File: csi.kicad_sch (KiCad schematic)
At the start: 38 parts, among them J6 WE_68715014522, J7 WE_68715014022, T8 BSS138APW, U4 PCA9547BS,118

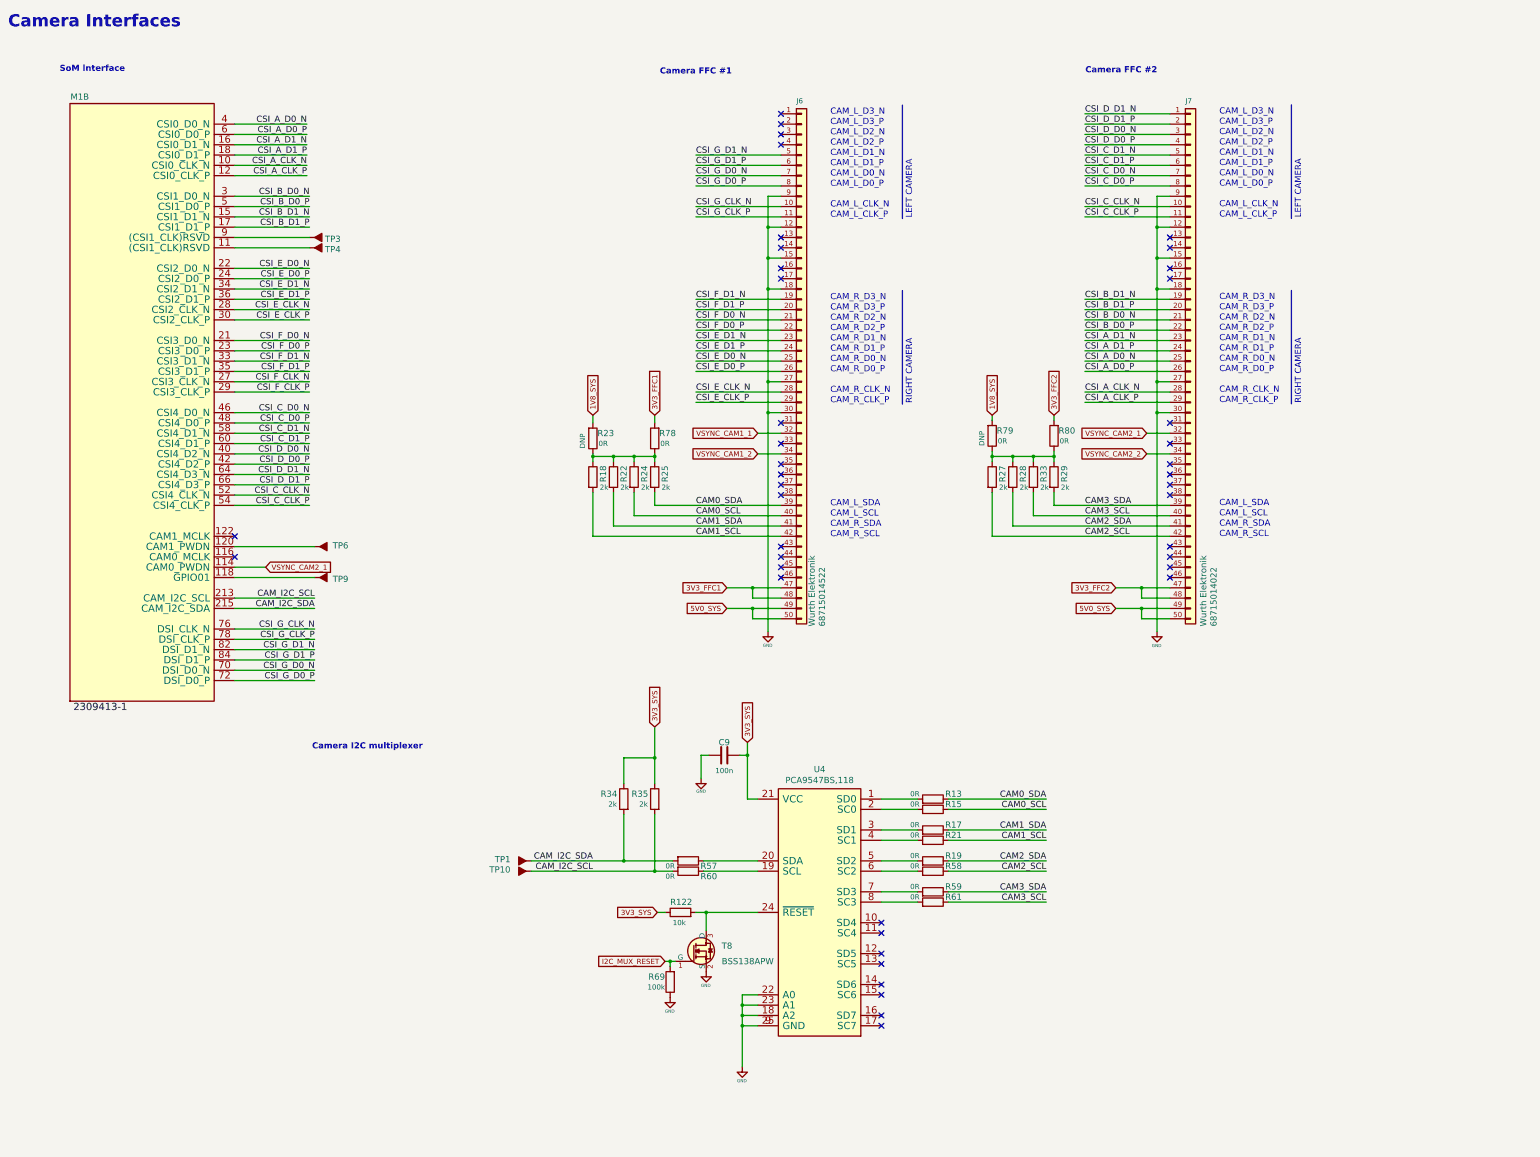
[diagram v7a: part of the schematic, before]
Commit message: Standardize components
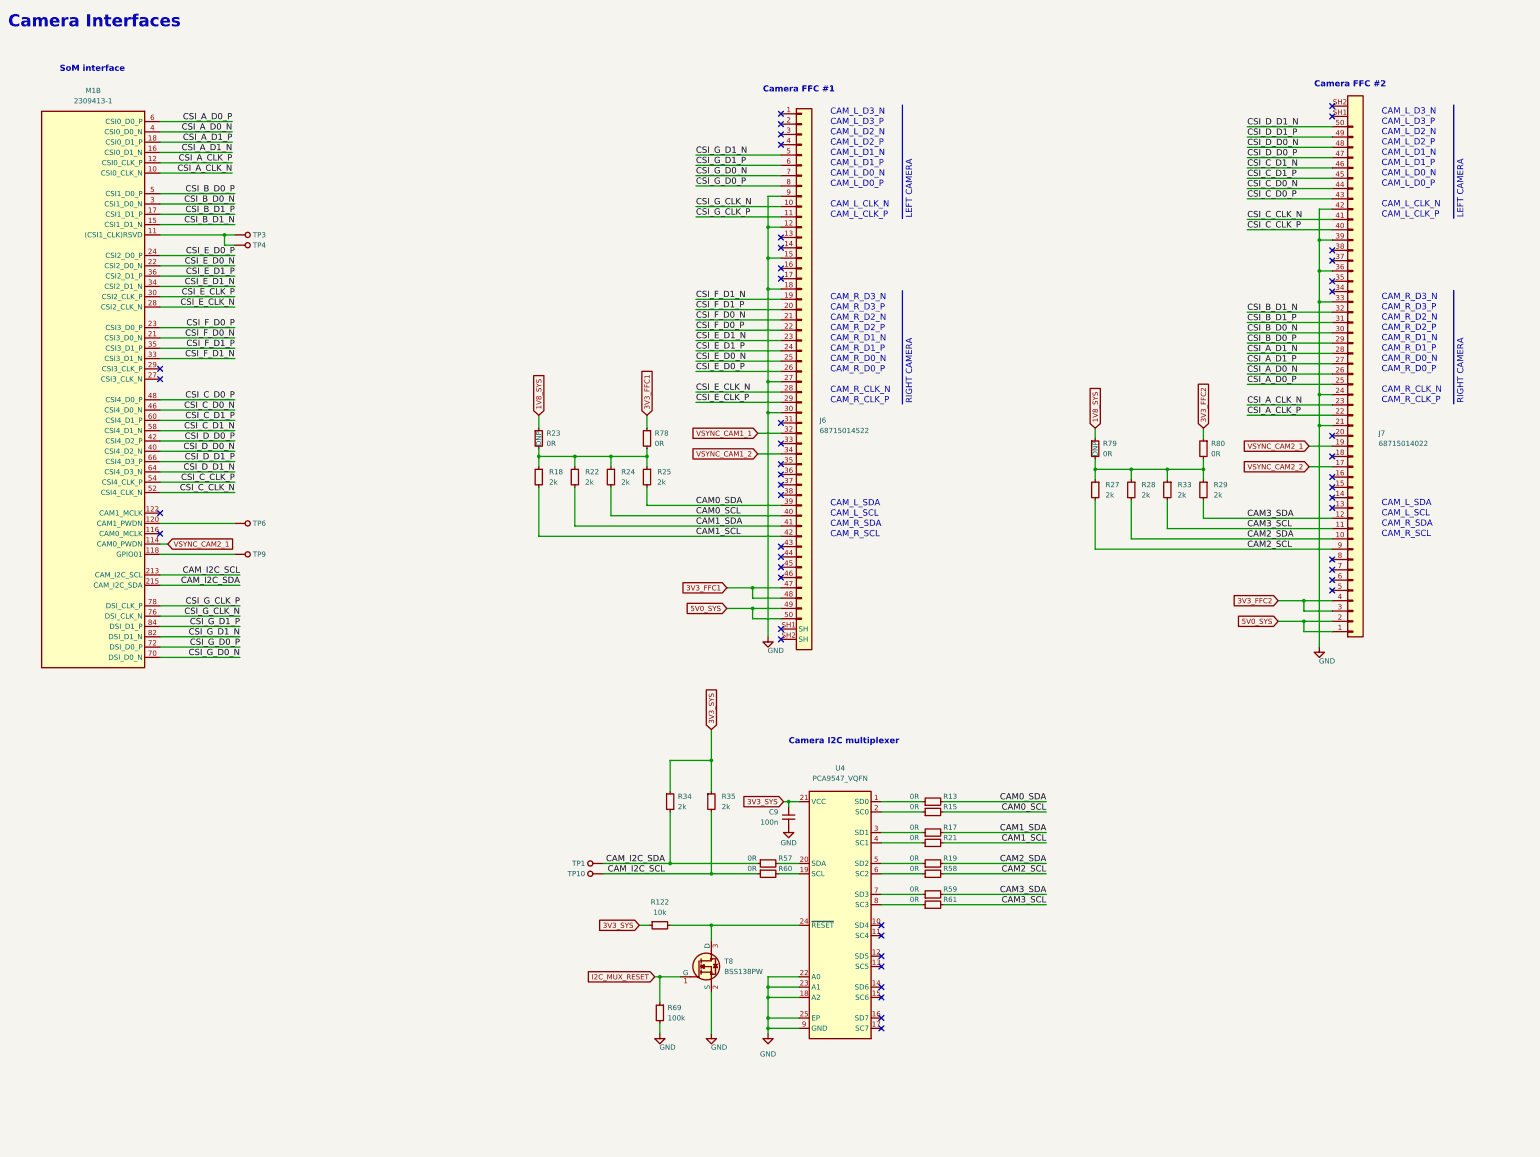
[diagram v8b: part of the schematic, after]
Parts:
- removed J6: WE_68715014522, jetson-nano-baseboard-footprints:WE_68715014522_ONE-SIDE, symbol jetson-nano-baseboard:WE_68715014522
- removed J7: WE_68715014022, jetson-nano-baseboard-footprints:WE_68715014022, symbol jetson-nano-baseboard:WE_68715014022
- removed U4: PCA9547BS,118, jetson-nano-baseboard-footprints:HVQFN24, symbol jetson-nano-baseboard:PCA9547BS,118
- added J6: Conn_FFC_WE_68715014522_ONE-SIDE, antmicro-footprints:Conn_FFC_WE_68715014x22, symbol antmicroFCCConnectors:Conn_FFC_WE_68715014522_ONE-SIDE
- added J7: Conn_FFC_WE_68715014022_ONE-SIDE, antmicro-footprints:Conn_FFC_WE_68715014x22, symbol antmicroFCCConnectors:Conn_FFC_WE_68715014022_ONE-SIDE
- added U4: PCA9547_VQFN, antmicro-footprints:VQFN-24-1EP_3.8x3.8x1.0mm_P0.5mm, symbol antmicroLogicSignalSwitchesMultiplexersDecoders:PCA9547_VQFN
- C9: footprint jetson-nano-baseboard-footprints:0402-cap -> antmicro-footprints:C_0402_1005Metric; symbol jetson-nano-baseboard:C_100n_0402 -> antmicroCapacitors0402:C_100n_0402; Author (none) -> Antmicro; Dielectric (none) -> X5R; License (none) -> Apache-2.0; MPN 0402X104K6R3CT -> GRM155R61H104KE14D; Manufacturer Walsin -> Murata; Voltage (none) -> 50V
- M1: value ~ -> Jetson-Nano-new-release; footprint jetson-nano-baseboard-footprints:jetson-nano-connector -> antmicro-footprints:TE_2309413; symbol jetson-nano-baseboard:Jetson-Nano-new-release -> antmicroSoMConnectors:Jetson-Nano-new-release; Author (none) -> Antmicro; License (none) -> Apache-2.0; Manufacturer TE -> TE Connectivity
- R122: footprint jetson-nano-baseboard-footprints:0402-res -> antmicro-footprints:R_0402_1005Metric; symbol jetson-nano-baseboard:R_10k_0402 -> antmicroResistors0402:R_10k_0402; Author (none) -> Antmicro; License (none) -> Apache-2.0; MPN CRCW040210K0FKEDHP -> CR0402-FX-1002GLF; Manufacturer VISHAY -> Bourns; Tolerance (none) -> 1%
- R13, R15, R17, R19, R21, R23, R57, R58, R59, R60, R61, R78, R79, R80: footprint jetson-nano-baseboard-footprints:0402-res -> antmicro-footprints:R_0402_1005Metric; symbol jetson-nano-baseboard:R_0R_0402 -> antmicroResistors0402:R_0R_0402; Author (none) -> Antmicro; Current (none) -> 1A; License (none) -> Apache-2.0; Manufacturer PANASONIC -> Panasonic
- R18, R22, R24, R25, R27, R28, R29, R33, R34, R35: footprint jetson-nano-baseboard-footprints:0402-res -> antmicro-footprints:R_0402_1005Metric; symbol jetson-nano-baseboard:R_2k_0402 -> antmicroResistors0402:R_2k_0402; Author (none) -> Antmicro; License (none) -> Apache-2.0; MPN CRCW04022K00FKED -> CR0402-FX-2001GLF; Manufacturer VISHAY -> Bourns; Tolerance (none) -> 1%
- R69: footprint jetson-nano-baseboard-footprints:0402-res -> antmicro-footprints:R_0402_1005Metric; symbol jetson-nano-baseboard:R_100k_0402 -> antmicroResistors0402:R_100k_0402; Author (none) -> Antmicro; License (none) -> Apache-2.0; MPN CRCW0402100KFKEDHP -> CR0402-FX-1003GLF; Manufacturer VISHAY -> Bourns; Tolerance (none) -> 1%
- T8: value BSS138APW -> BSS138PW; footprint jetson-nano-baseboard-footprints:SC70-3 -> antmicro-footprints:SC70-3; symbol jetson-nano-baseboard:BSS138APW -> antmicroTransistorsFETsMOSFETsSingle:BSS138PW; Author (none) -> Antmicro; License (none) -> Apache-2.0; Manufacturer ON Semiconductor -> Nexperia
- TP1, TP10, TP3, TP4, TP6, TP9: value ~ -> TP_1.5mm_SMD; footprint jetson-nano-baseboard-footprints:TP-R-1.5 -> antmicro-footprints:TP_SMD_1.5mm; symbol jetson-nano-baseboard:Testpad -> antmicroTestPoints:TP_1.5mm_SMD; Author (none) -> Antmicro; License (none) -> Apache-2.0
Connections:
- net 1V8_SYS: now also R23.1, R79.1; no longer R23.2, R79.2
- net 3V3_FFC1: now also R78.1, J6.47, J6.48; no longer R78.2
- net 3V3_FFC2: now also R80.1, J7.3, J7.4; no longer R80.2
- net 3V3_SYS: now also U4.21 (VCC)
- net 5V0_SYS: now also J6.49, J6.50, J7.1, J7.2
- net CAM0_SCL: now also R15.2, J6.40; no longer R15.1
- net CAM0_SDA: now also R13.2, J6.39; no longer R13.1
- net CAM1_SCL: now also R21.2, J6.42; no longer R21.1
- net CAM1_SDA: now also R17.2, J6.41; no longer R17.1
- net CAM2_SCL: now also R58.2, J7.9; no longer R58.1
- net CAM2_SDA: now also R19.2, J7.10; no longer R19.1
- net CAM3_SCL: now also R61.2, J7.11; no longer R61.1
- net CAM3_SDA: now also R59.2, J7.12; no longer R59.1
- net CAM_I2C_SCL: now also R60.1; no longer R60.2
- net CAM_I2C_SDA: now also R57.1; no longer R57.2
- net CSI_A_CLK_N: now also J7.23
- net CSI_A_CLK_P: now also J7.22
- net CSI_A_D0_N: now also J7.26
- net CSI_A_D0_P: now also J7.25
- net CSI_A_D1_N: now also J7.28
- net CSI_A_D1_P: now also J7.27
- net CSI_B_D0_N: now also J7.30
- net CSI_B_D0_P: now also J7.29
- net CSI_B_D1_N: now also J7.32
- net CSI_B_D1_P: now also J7.31
- net CSI_C_CLK_N: now also J7.41
- net CSI_C_CLK_P: now also J7.40
- net CSI_C_D0_N: now also J7.44
- net CSI_C_D0_P: now also J7.43
- net CSI_C_D1_N: now also J7.46
- net CSI_C_D1_P: now also J7.45
- net CSI_D_D0_N: now also J7.48
- net CSI_D_D0_P: now also J7.47
- net CSI_D_D1_N: now also J7.50
- net CSI_D_D1_P: now also J7.49
- net CSI_E_CLK_N: now also J6.28
- net CSI_E_CLK_P: now also J6.29
- net CSI_E_D0_N: now also J6.25
- net CSI_E_D0_P: now also J6.26
- net CSI_E_D1_N: now also J6.23
- net CSI_E_D1_P: now also J6.24
- net CSI_F_D0_N: now also J6.21
- net CSI_F_D0_P: now also J6.22
- net CSI_F_D1_N: now also J6.19
- net CSI_F_D1_P: now also J6.20
- net CSI_G_CLK_N: now also J6.10
- net CSI_G_CLK_P: now also J6.11
- net CSI_G_D0_N: now also J6.7
- net CSI_G_D0_P: now also J6.8
- net CSI_G_D1_N: now also J6.5
- net CSI_G_D1_P: now also J6.6
- net GND: now also R69.2, J6.12, J6.15, J6.18, J6.27, J6.30, J6.9, J7.21, J7.24, J7.33, J7.36, J7.39, J7.42, U4.18 (A2), U4.22 (A0), U4.23 (A1), U4.25 (EP), U4.9 (GND); no longer R69.1
- net I2C_MUX_RESET: now also R69.1; no longer R69.2
- net VSYNC_CAM1_1: now also J6.32
- net VSYNC_CAM1_2: now also J6.34
- net VSYNC_CAM2_1: now also J7.19
- net VSYNC_CAM2_2: now also J7.17
- net at M1.11 ((CSI1_CLK)RSVD), TP4.1: now also M1.9 ((CSI1_CLK)RSVD), TP3.1
- net at R18.1, R22.1, R24.1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: now also R23.2, R78.2; no longer R23.1, R78.1
- net at R27.1, R28.1, R29.1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: now also R79.2, R80.2; no longer R79.1, R80.1
- net at R122.2, T8.3 (D): now also U4.24 (~{RESET})
- net CSI_F_CLK_N: no longer names the net of M1.27 (CSI3_CLK_N)
- net CSI_F_CLK_P: no longer names the net of M1.29 (CSI3_CLK_P)
- new net: R13.1, U4.1 (SD0)
- new net: R15.1, U4.2 (SC0)
- new net: R17.1, U4.3 (SD1)
- new net: R21.1, U4.4 (SC1)
- new net: R19.1, U4.5 (SD2)
- new net: R58.1, U4.6 (SC2)
- new net: R59.1, U4.7 (SD3)
- new net: R61.1, U4.8 (SC3)
- new net: R57.2, U4.20 (SDA)
- new net: R60.2, U4.19 (SCL)
- no-connect marks 42 -> 48
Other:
- moved on the sheet: C9, R122, R13, R15, R17, R18, R19, R21, R22, R23, R24, R25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
